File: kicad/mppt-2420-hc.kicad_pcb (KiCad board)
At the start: 4 copper layers, 100 x 100 mm, 172 parts, among them J1 MKDS 5/ 2-9,5, J2 MKDS 5/ 2-9,5, J3 MKDS 5/ 2-9,5, J4 8P8C, J5 8P8C, J6 JST PH, J7 UEXT, P1 CONN_01X02, Q1 IPA045N10N3G, Q2 IPA045N10N3G, Q3 IPA045N10N3G, Q4 BUK98180-100A, Q7 IPA045N10N3G, T1 BC846B, T10 BC846B, T2 BC846B, T3 BC846B, T4 BC856B, T5 BC846B, U1 LM5107, U2 STM32G431CBTx, U3 INA186, U4 LMR16006X, U5 INA186, U6 W25Q80DVS, U7 TCAN334, Y1 8MHz

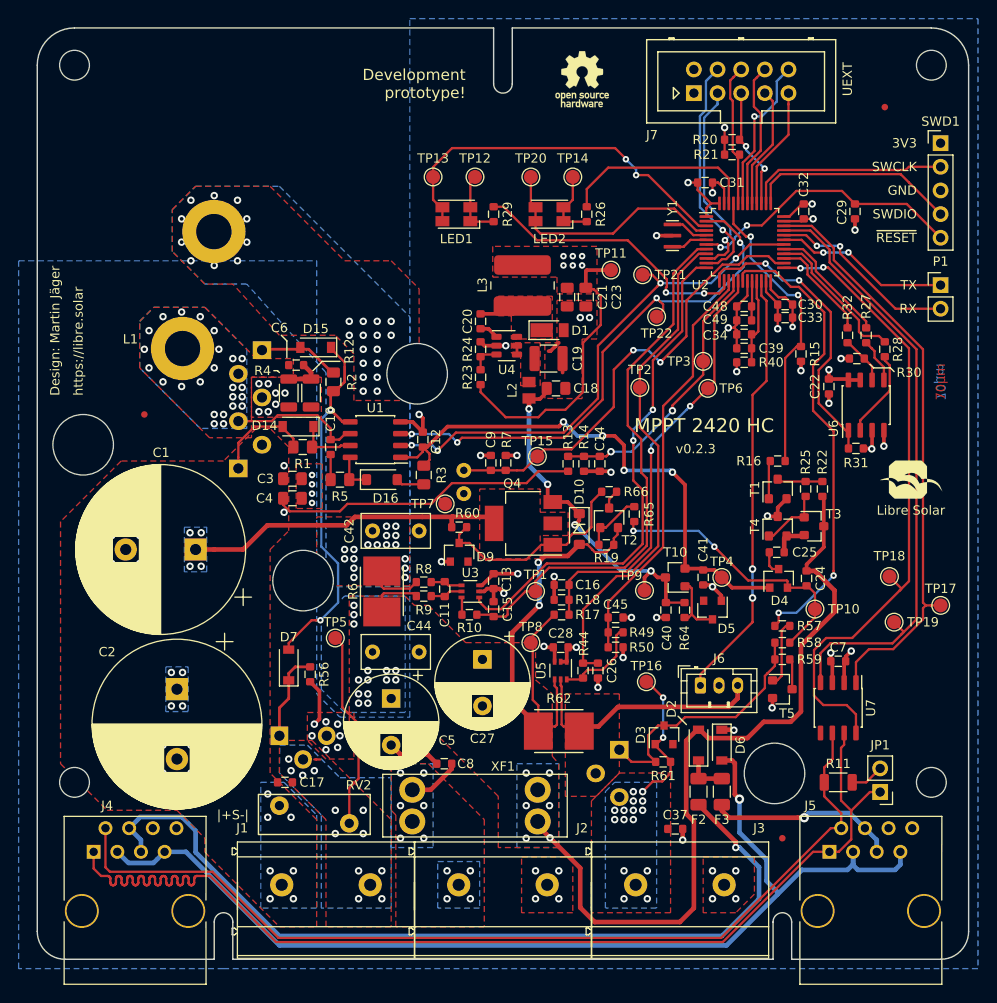
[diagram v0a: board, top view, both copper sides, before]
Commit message: initial 48v LV side kicad update:
migrated files to KiCad 6

replaced LV side current amp ic (60v)

replaced caps in LV (63v)

removed HV rail supply option
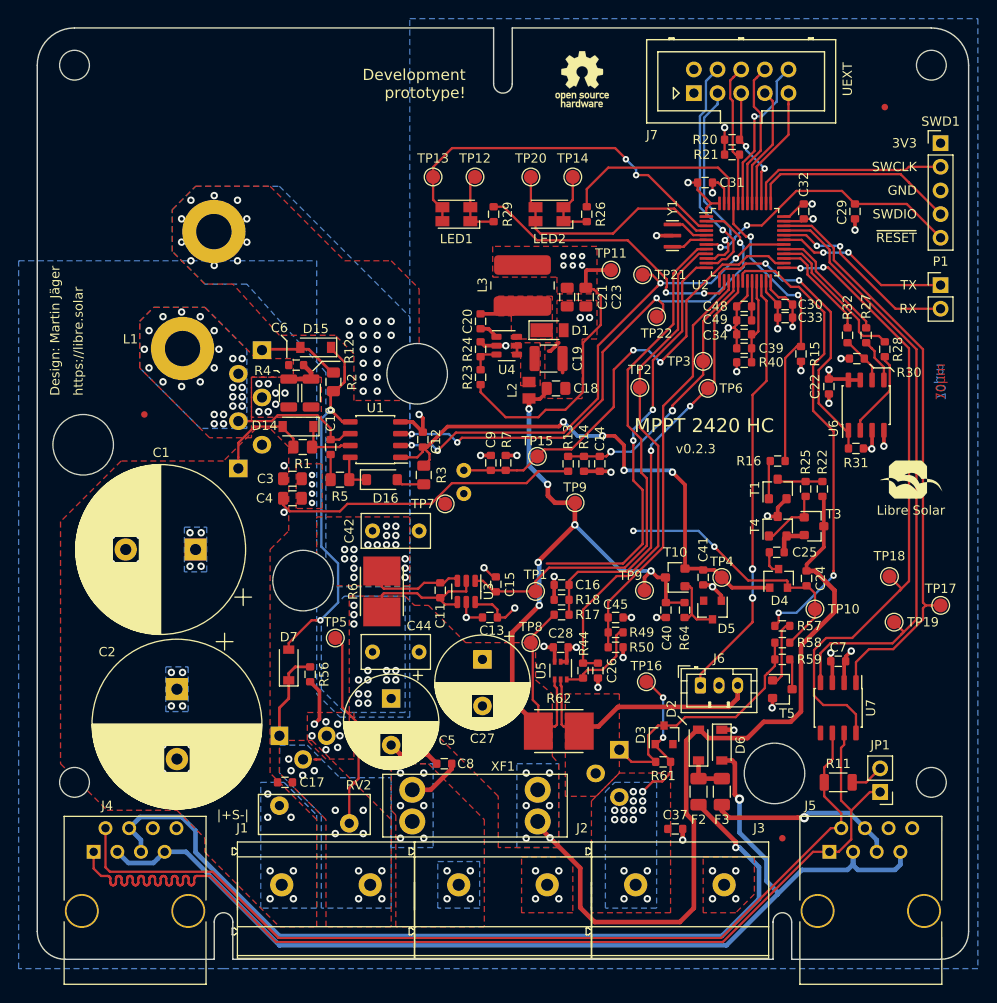
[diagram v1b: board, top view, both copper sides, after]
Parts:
- removed D10: 1N4148, LibreSolar:D_SOD-123
- removed D9: 47V, Diode_SMD:D_SOT-23_ANK
- removed Q4: BUK98180-100A, Package_TO_SOT_SMD:SOT-223-3_TabPin2
- removed R10, R66: 1k, LibreSolar:R_0603_1608
- removed R19: 10k, LibreSolar:R_0603_1608
- removed R60, R65: 100k, LibreSolar:R_0603_1608
- removed R8, R9: 10R, LibreSolar:R_0603_1608
- removed T2: BC846B, LibreSolar:SOT-23
- added TP9: 1.5mm, TestPoint:TestPoint_Pad_D1.5mm, F.Cu at (157.7, 91.0)
- C1, C2: value 390µF -> 560µF
- U3: value INA186 -> MPQ8112; footprint Package_TO_SOT_SMD:SOT-363_SC-70-6 -> Package_TO_SOT_SMD:TSOT-23-6
- moved C13 3.92 mm to (148.6, 103.3), turned to 180 degrees
- moved C15 2.67 mm to (149.2, 99.7)
- moved C11 0.50 mm to (143.3, 100.4)
- moved U3 0.44 mm to (146.1, 100.5), turned to -90 degrees
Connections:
- net /MCU/ADC12_IN2 renamed /Load switch/I_LOAD
- net /MCU/ADC1_IN12 renamed /DC/DC/V_DCDC_L
- net /MCU/ADC1_IN15 renamed /DC/DC/V_DCDC_H
- net /MCU/COMP2_INP renamed /Load switch/I_LOAD_COMP
- net /MCU/GPIOB_2 renamed /Load switch/LOAD_DIS
- net /MCU/~RESET renamed /MCU/~{RESET}
- net /Power supply/CP_PWM renamed /MCU/TIM8_CH2
- C11 pad 1: Net-(C11-Pad1) -> /DC/DC/SHUNT_DCDC_P
- C11 pad 2: Net-(C11-Pad2) -> VBUS
- C15 pad 1: /MCU/ADC12_IN1 -> /DC/DC/I_DCDC
- C18 pad 1: /Power supply/SUPPLY_INPUT -> VBUS
- C40 pad 1: /Power supply/SUPPLY_INPUT -> VBUS
- J4 pad 6: Net-(J4-Pad6) -> unconnected-(J4-Pad6)
- J4 pad 8: Net-(J4-Pad8) -> unconnected-(J4-Pad8)
- J5 pad 6: Net-(J5-Pad6) -> unconnected-(J5-Pad6)
- J5 pad 8: Net-(J5-Pad8) -> unconnected-(J5-Pad8)
- L2 pad 1: /Power supply/SUPPLY_INPUT -> VBUS
- R64 pad 2: /Power supply/SUPPLY_INPUT -> VBUS
- T10 pad 3: /Power supply/SUPPLY_INPUT -> VBUS
- TP1 pad 1: /MCU/ADC12_IN1 -> /DC/DC/I_DCDC
- U2 pad 8: /MCU/ADC12_IN1 -> /DC/DC/I_DCDC
- U3 pad 1: /MCU/DAC1 -> /DC/DC/I_DCDC
- U3 pad 2: GND -> VBUS
- U3 pad 3: +3V3 -> /DC/DC/SHUNT_DCDC_P
- U3 pad 4: Net-(C11-Pad1) -> VBUS
- U3 pad 5: Net-(C11-Pad2) -> GND
- U3 pad 6: Net-(R10-Pad1) -> +3V3
- U7 pad 5: Net-(U7-Pad5) -> unconnected-(U7-Pad5)
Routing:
- net /MCU/ADC12_IN1: track 59.2 -> 0.00 mm
- net /DC/DC/I_DCDC: track 0.00 -> 58.4 mm
- net VBUS: track 142.2 -> 184.2 mm, vias 22 -> 26
- net /Power supply/SUPPLY_INPUT: track 38.7 -> 0.00 mm, vias 4 -> 0
- net /DCDC_HV+: track 69.7 -> 34.6 mm
- net Net-(D9-Pad1): track 23.0 -> 0.00 mm
- net /MCU/DAC1: track 55.2 -> 45.1 mm
- net Net-(R19-Pad2): track 6.49 -> 0.00 mm
- net /DC/DC/SHUNT_DCDC_P: track 6.07 -> 10.8 mm
- net Net-(C11-Pad2): track 3.50 -> 0.00 mm
- net Net-(C11-Pad1): track 3.44 -> 0.00 mm
- net Net-(R66-Pad1): track 2.08 -> 0.00 mm
- net Net-(R10-Pad1): track 1.87 -> 0.00 mm
- net +3V3: track 71.5 -> 72.7 mm
- net /Load switch/CP_OUT: track 30.3 -> 29.3 mm
- added copper zone on In2.Cu, net +3V3
- added copper zone on In2.Cu, net /DC/DC/SHUNT_DCDC_P
- added copper zone on In1.Cu, net /DC/DC/SW_NODE
- added copper zone on In2.Cu, net /DC/DC/SW_NODE
- added copper zone on In2.Cu, net /DCDC_HV+
- added copper zone on In1.Cu, net GND
- removed copper zone on 3V3, net +3V3
- removed copper zone on 3V3, net /DC/DC/SHUNT_DCDC_P
- removed copper zone on 3V3, net /DC/DC/SW_NODE
- removed copper zone on GND, net /DC/DC/SW_NODE
- removed copper zone on 3V3, net /DCDC_HV+
- removed copper zone on GND, net GND
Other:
- net class Default removed
- net class Power removed
- board text added: "~{RESET}"
- board text removed: "~RESET"

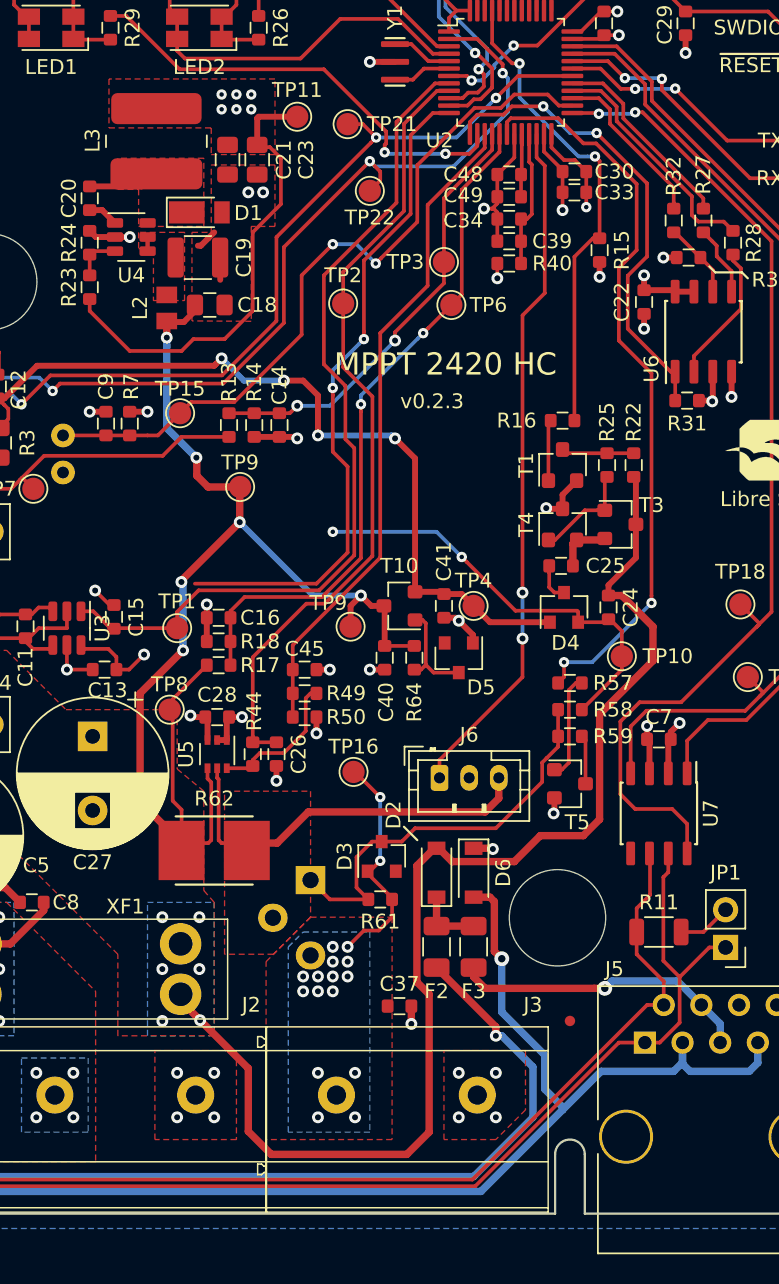
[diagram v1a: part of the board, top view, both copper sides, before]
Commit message: removed load terminal & circuit
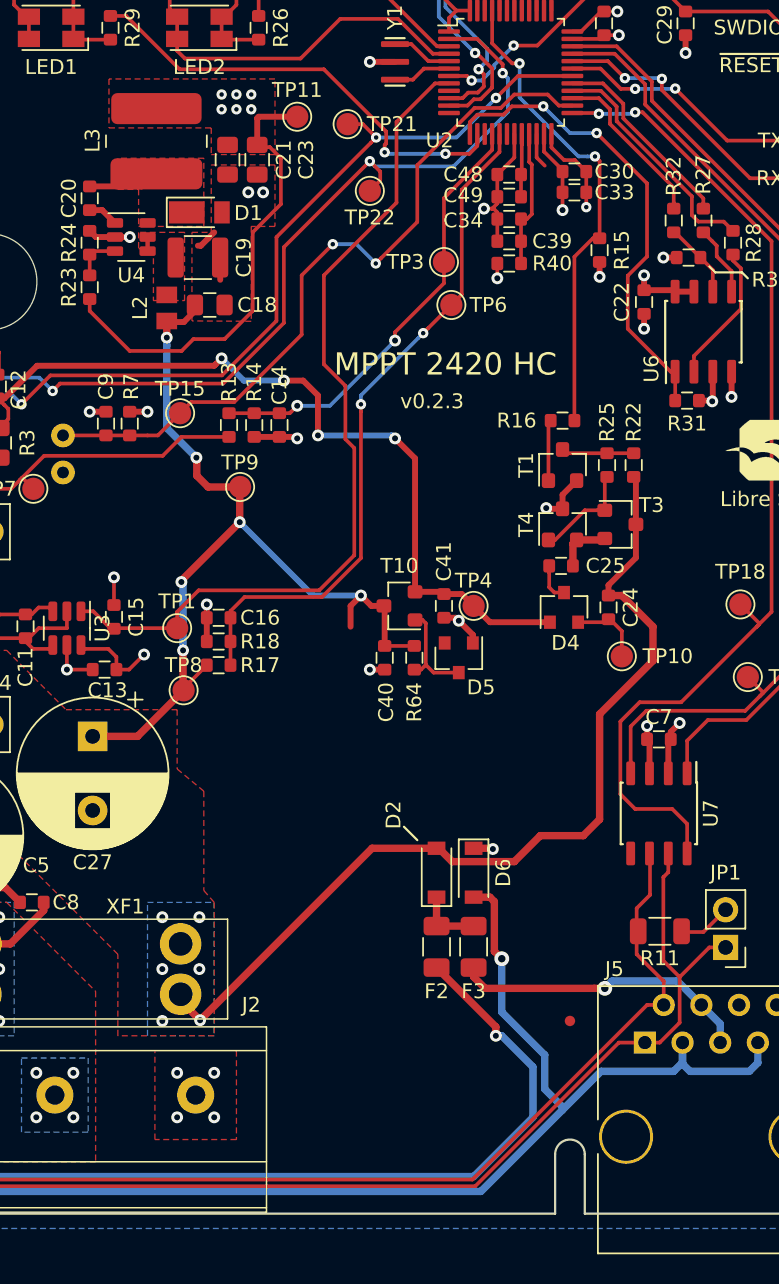
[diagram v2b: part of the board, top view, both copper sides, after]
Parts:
- removed C26, C37, C45: 10nF, LibreSolar:C_0603_1608
- removed C28: 100nF, LibreSolar:C_0603_1608
- removed D3: 12V, Diode_SMD:D_SOT-23_ANK
- removed J3: MKDS 5/ 2-9,5, LibreSolar:Phoenix_Contact_MKDS_5-2-9,5
- removed J6: JST PH, Connector_JST:JST_PH_B3B-PH-K_1x03_P2.00mm_Vertical
- removed Q7: IPA045N10N3G, LibreSolar:TO-220-3_Horizontal_BottomHeatsink
- removed R44, R57: 2.2k, LibreSolar:R_0603_1608
- removed R49, R59: 10k, LibreSolar:R_0603_1608
- removed R50: 8.2k, LibreSolar:C_0603_1608
- removed R58: 100k, LibreSolar:R_0603_1608
- removed R61: 1M, LibreSolar:R_0603_1608
- removed R62: 2m, LibreSolar:R_Bourns_CRE2512
- removed T5: BC846B, LibreSolar:SOT-23
- removed TP16, TP2: 1.5mm, TestPoint:TestPoint_Pad_D1.5mm
- removed the TP9 at (165.2, 100.4)
- removed U5: INA186, Package_TO_SOT_SMD:SOT-363_SC-70-6
- R11: footprint LibreSolar:R_1206_3216 -> Resistor_SMD:R_1206_3216Metric
- moved TP8 1.61 mm to (153.9, 104.7)
- moved R11 0.08 mm to (186.1, 121.0)
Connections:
- net /Load switch/CP_OUT renamed /Power supply/CP_OUT
- U2 pad 15: /Load switch/I_LOAD_COMP -> /MCU/COMP2_INP
- U2 pad 18: /Load switch/LOAD_DIS -> /MCU/GPIOB_2
- U2 pad 22: /PWR_INFO -> /MCU/GPIOB_10
- U2 pad 9: /Load switch/I_LOAD -> /MCU/ADC12_IN2
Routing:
- net /Load switch/I_LOAD: track 53.9 -> 0.00 mm
- net /Load switch/LOAD_DIS: track 50.3 -> 0.00 mm, vias 2 -> 0
- net /PWR_INFO: track 46.6 -> 0.00 mm, vias 2 -> 0
- net /MCU/DAC1: track 45.1 -> 0.00 mm, vias 2 -> 0
- net VBUS: track 184.2 -> 139.4 mm
- net /Load switch/I_LOAD_COMP: track 44.7 -> 0.00 mm
- net Net-(D3-Pad1): track 27.6 -> 0.00 mm
- net /MEAS_LV+: track 26.5 -> 0.00 mm
- net /Power supply/CP_OUT: track 29.3 -> 5.06 mm, vias 2 -> 0
- net /LOAD+: track 15.6 -> 0.00 mm, vias 17 -> 0
- net Net-(R44-Pad1): track 9.67 -> 0.00 mm
- net GND: track 82.4 -> 74.5 mm, vias 64 -> 54
- net Net-(R57-Pad2): track 7.14 -> 0.00 mm
- net Net-(R59-Pad1): track 3.30 -> 0.00 mm
- net +3V3: track 72.7 -> 70.1 mm, vias 17 -> 16
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- removed copper zone on B.Cu, net /LOAD+
- removed copper zone on F.Cu, net /LOAD+
- removed copper zone on F.Cu, net /MEAS_LV+

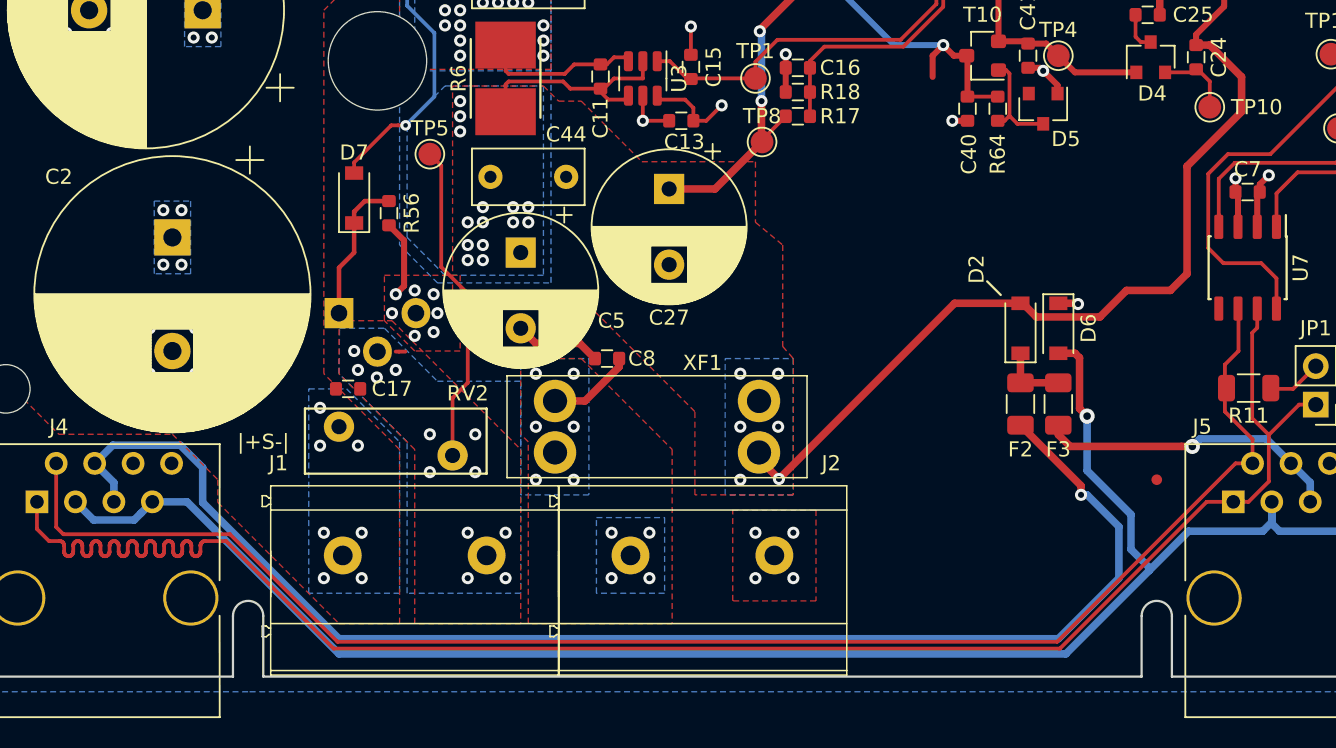
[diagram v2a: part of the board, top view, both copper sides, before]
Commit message: major changes
removed Load terminal

changed to 6.3x32mm fuse pcb holder

added LibreSolar kicad footprint library locally
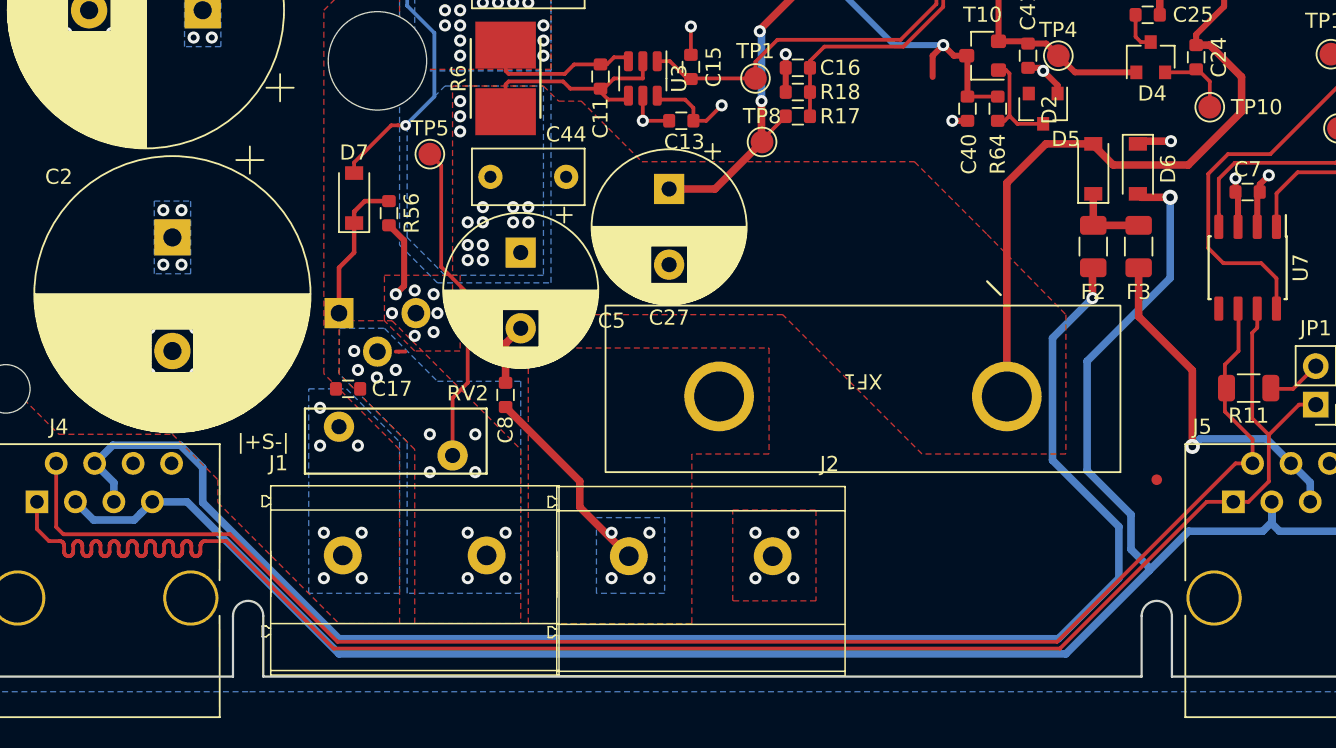
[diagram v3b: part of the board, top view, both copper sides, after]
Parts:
- XF1: footprint LibreSolar:Keystone-Fuse-3557-2 -> LibreSolar:Eaton_S-400
- moved XF1 13.7 mm to (160.6, 121.5)
- moved D6 11.8 mm to (178.8, 106.5)
- moved F3 11.7 mm to (178.8, 111.6)
- moved D2 11.6 mm to (175.8, 106.5)
- moved F2 11.5 mm to (175.8, 111.6)
- moved C8 7.12 mm to (137.0, 121.4), turned to 90 degrees
- moved J2 0.12 mm to (145.1, 132.1)
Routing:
- net VBUS: track 139.4 -> 124.3 mm, vias 26 -> 20
- net /CAN_GND: track 114.9 -> 128.3 mm
- net /CAN/CAN_PWR1: track 92.6 -> 103.0 mm
- net /BAT+: track 5.71 -> 13.2 mm, vias 10 -> 4
- net /CAN/CAN_PWR2: track 20.3 -> 23.7 mm
- net GND: track 74.5 -> 73.7 mm
- net Net-(D2-Pad1): track 4.45 -> 5.08 mm
